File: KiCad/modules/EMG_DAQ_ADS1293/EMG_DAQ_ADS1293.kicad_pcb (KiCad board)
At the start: 2 copper layers, 15 x 9.5 mm, 27 parts, among them J1 Conn_01x01_Pin, J10 Conn_01x01_Pin, J11 Conn_01x01_Pin, J12 Conn_01x01_Pin, J13 Conn_01x01_Pin, J14 Conn_01x01_Pin, J15 Conn_01x01_Pin, J16 Conn_01x01_Pin, J2 Conn_01x01_Pin, J3 Conn_01x01_Pin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

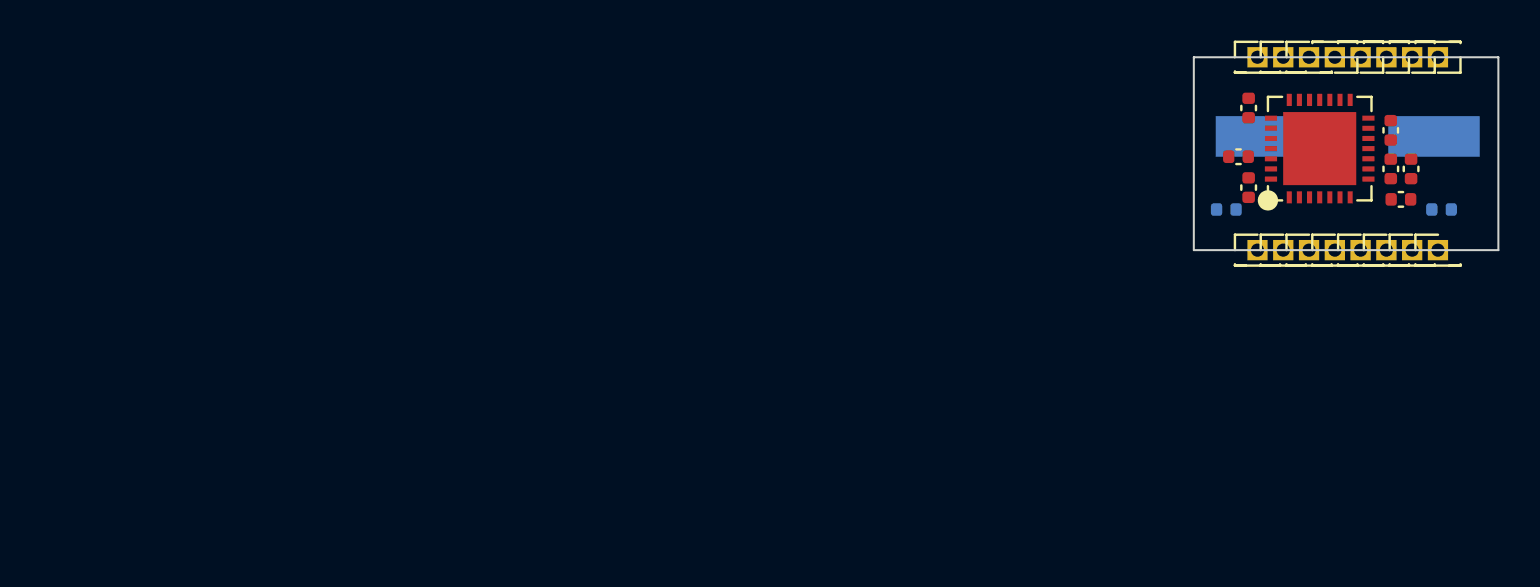
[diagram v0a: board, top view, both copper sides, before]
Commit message: reshaped the modules boards sizes
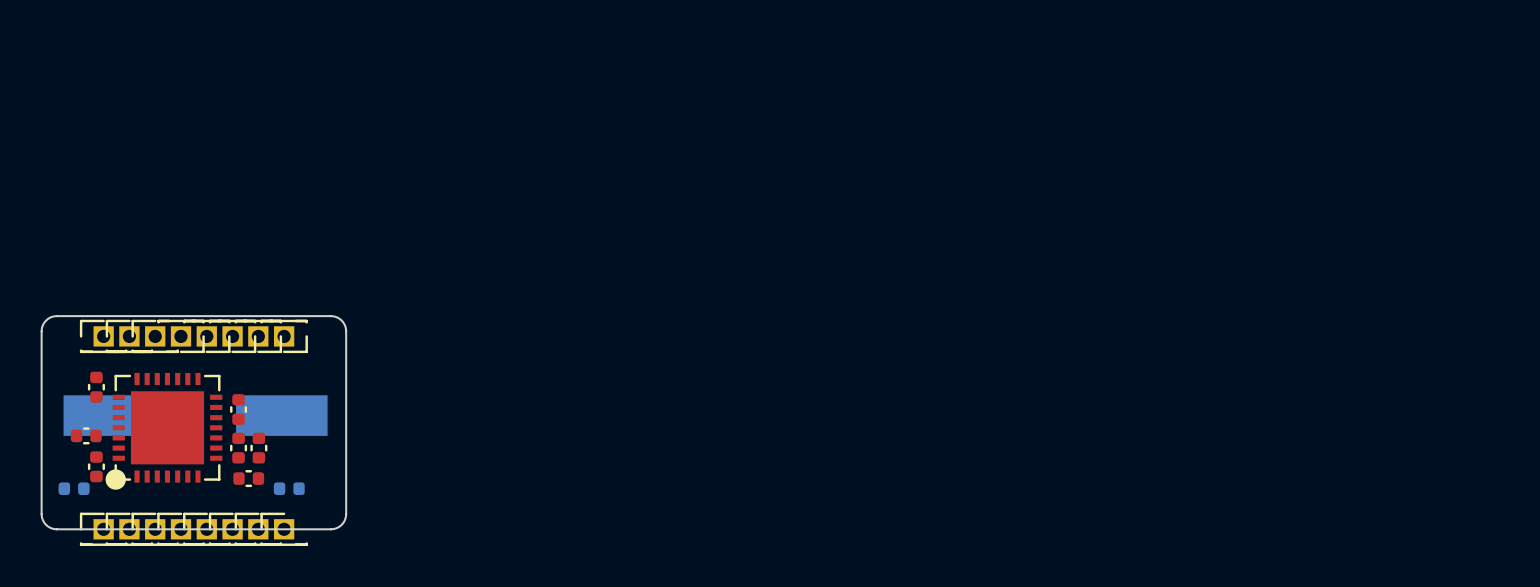
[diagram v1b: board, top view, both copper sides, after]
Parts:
- moved J11 58.5 mm to (104.4, 100.0)
- moved J12 58.5 mm to (98.1, 100.0)
- moved J16 58.5 mm to (104.4, 109.5)
- moved J3 58.5 mm to (98.1, 109.5)
- moved J6 58.5 mm to (101.9, 109.5)
- moved J9 58.5 mm to (101.9, 100.0)
- moved J10 58.5 mm to (103.2, 100.0)
- moved J14 58.5 mm to (96.8, 100.0)
- moved J15 58.5 mm to (103.2, 109.5)
- moved J2 58.5 mm to (96.8, 109.5)
- moved J4 58.5 mm to (99.4, 109.5)
- moved J5 58.5 mm to (100.6, 109.5)
- moved J7 58.5 mm to (99.4, 100.0)
- moved J8 58.5 mm to (100.6, 100.0)
- moved J1 58.5 mm to (95.6, 109.5)
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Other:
- board size 15 x 9.5 mm -> 15 x 10.5 mm
- copper layers 2 -> 4

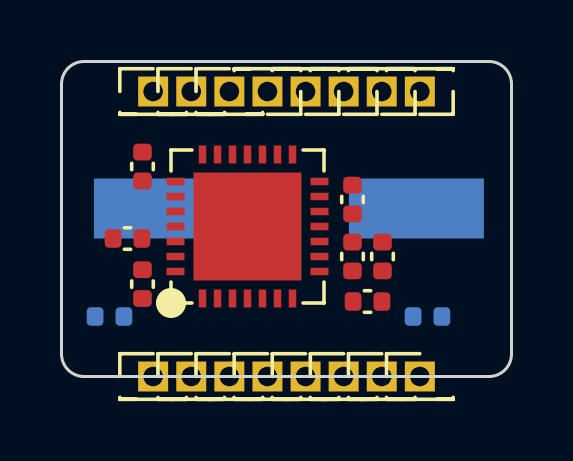
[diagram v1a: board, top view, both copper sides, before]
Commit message: some cleaning + edge plating dry electrode
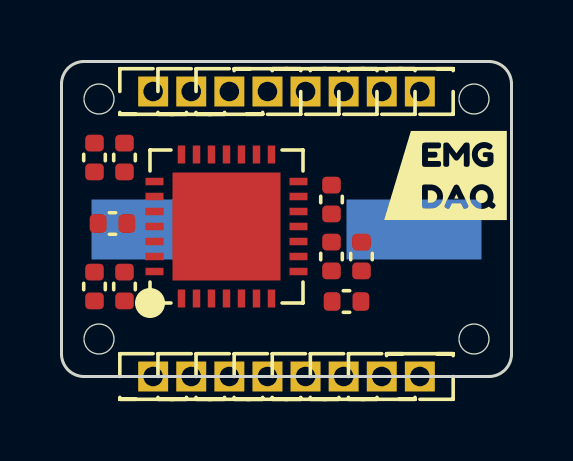
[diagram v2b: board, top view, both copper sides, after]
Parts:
- added kibuzzard-6569F40D: G***, kibuzzard-6569F40D, F.Cu at (105.3, 102.8)
- C1, C2: moved to F.Cu
- moved C2 11.1 mm to (93.6, 106.5), turned to -90 degrees
- moved C4 2.92 mm to (93.6, 102.2), turned to -90 degrees
- moved C3 2.25 mm to (94.2, 104.4), turned to 0 degrees
- moved C1 1.12 mm to (94.6, 106.5), turned to 90 degrees
- moved Y1 0.70 mm to (100.0, 104.6)
- moved C6 0.70 mm to (101.5, 105.5)
- moved C7 0.70 mm to (101.5, 103.6)
- moved R1 0.70 mm to (102.0, 107.0)
- moved R2 0.70 mm to (102.5, 105.5)
- moved U1 0.70 mm to (98.0, 104.5)
- moved C5 0.67 mm to (94.6, 102.2)
- turned J16 to 180 degrees
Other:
- outline, holes or cut-outs redrawn
- board text added: "By Aightech"

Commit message: finished rooting emgdaq + schematic commod
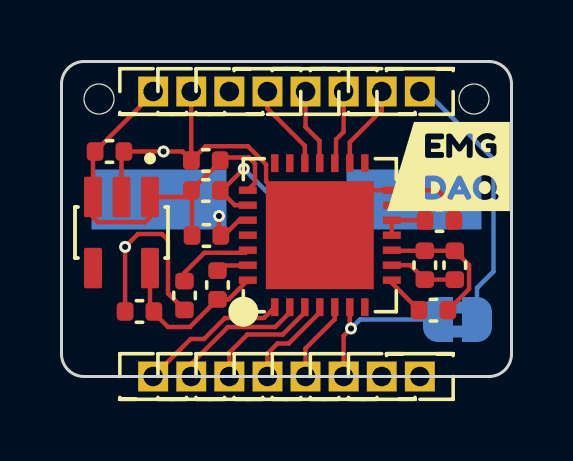
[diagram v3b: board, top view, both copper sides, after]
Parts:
- added C8: 1uF, Capacitor_SMD:C_0402_1005Metric, F.Cu at (95.1, 107.3)
- added C9: 1uF, Capacitor_SMD:C_0402_1005Metric, F.Cu at (94.1, 102.0)
- added JP2: SolderJumper_2_Bridged, Jumper:SolderJumper-2_P1.3mm_Bridged2Bar_RoundedPad1.0x1.5mm, B.Cu at (105.7, 107.6)
- added U2: AP2112K-3.3TRG1, 00_custom-footprints:SOT95P285X140-5N, F.Cu at (94.5, 104.7)
- moved J1 9.83 mm to (98.1, 100.0)
- moved J8 9.58 mm to (101.9, 109.5), turned to 0 degrees
- moved J12 5.08 mm to (103.2, 100.0)
- moved J7 5.08 mm to (104.4, 100.0)
- moved C4 3.87 mm to (97.3, 103.3), turned to 0 degrees
- moved C7 3.67 mm to (105.1, 104.3), turned to 0 degrees
- moved C3 3.16 mm to (97.3, 104.8)
- moved C6 3.12 mm to (104.6, 105.8)
- moved R2 3.12 mm to (105.6, 105.8)
- moved U1 3.12 mm to (101.1, 104.8)
- moved C1 3.10 mm to (97.7, 106.5)
- moved C2 3.01 mm to (96.6, 106.8)
- moved R1 2.91 mm to (104.9, 107.3)
- moved C5 2.71 mm to (97.3, 102.3), turned to 180 degrees
- moved J9 2.54 mm to (99.4, 100.0)
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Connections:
- net /+5VA renamed +3.3VA
- net Net-(J10-Pin_1) renamed /MOSI
- net Net-(J11-Pin_1) renamed /SCLK
- net Net-(J12-Pin_1) renamed /CSB
- net Net-(J9-Pin_1) renamed /MISO
- J1 pad 1: GND -> unconnected-(J1-Pin_1-Pad1)
- J13 pad 1: +5V -> +3.3V
- J7 pad 1: /in6 -> /extRef
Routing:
- net GND: track 0.00 -> 24.4 mm, vias 0 -> 2
- net +3.3V: track 0.00 -> 14.5 mm
- net /extRef: track 0.00 -> 8.96 mm
- net XTAL1: track 0.00 -> 8.31 mm, vias 0 -> 1
- net +3.3VA: track 0.00 -> 5.52 mm
- net /in6: track 0.00 -> 5.37 mm, vias 0 -> 1
- net /in1: track 0.00 -> 5.01 mm
- net /RLDINV: track 0.00 -> 4.58 mm
- net /in2: track 0.00 -> 4.51 mm
- net XTAL2: track 0.00 -> 4.16 mm, vias 0 -> 1
- net /in3: track 0.00 -> 3.96 mm
- net /in4: track 0.00 -> 3.17 mm
- net /MISO: track 0.00 -> 2.91 mm
- net /CSB: track 0.00 -> 2.83 mm
- net /cvref: track 0.00 -> 2.70 mm
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- added copper zone on In1.Cu, net GND
- added copper zone on In2.Cu, net GND
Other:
- outline, holes or cut-outs redrawn
- board text added: "Aightech"
- board text removed: "By Aightech"

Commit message: lot of updates on ads93,flex,commod,pad
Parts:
- removed kibuzzard-6569F40D: G***, kibuzzard-6569F40D
- added kibuzzard-658D7E24: G***, kibuzzard-658D7E24, F.Cu at (31.7, 31.6)
- U1: footprint 00_custom-footprints:ADS1293CISQE -> 00_Custom:ADS1293CISQE
- U2: footprint 00_custom-footprints:SOT95P285X140-5N -> 00_Custom:SOT95P285X140-5N
- moved J1 99.0 mm to (28.1, 30.0)
- moved J10 99.0 mm to (30.6, 30.0)
- moved J11 99.0 mm to (31.9, 30.0)
- moved J12 99.0 mm to (33.2, 30.0)
- moved J13 99.0 mm to (25.6, 30.0)
- moved J14 99.0 mm to (26.8, 30.0)
- moved J7 99.0 mm to (34.4, 30.0)
- moved J9 99.0 mm to (29.4, 30.0)
- moved C1 98.6 mm to (27.7, 37.0)
- moved C2 98.6 mm to (26.6, 37.3)
- moved C3 98.6 mm to (27.3, 35.3)
- moved C4 98.6 mm to (27.3, 33.8)
- moved C5 98.6 mm to (27.3, 32.8)
- moved C6 98.6 mm to (34.6, 36.3)
- moved C7 98.6 mm to (35.1, 34.8)
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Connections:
- J15 pad 1: unconnected-(J15-Pin_1-Pad1) -> /in4
- J16 pad 1: unconnected-(J16-Pin_1-Pad1) -> /in5
- J3 pad 1: /in2 -> /in1
- J4 pad 1: /in3 -> /in2
- J5 pad 1: /in4 -> /in2
- J6 pad 1: /in5 -> /in3
- J8 pad 1: /in6 -> /in3
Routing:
- net /in6: track 5.37 -> 3.34 mm
- net /in5: track 2.63 -> 4.19 mm
- net /in1: track 5.01 -> 6.20 mm
- net /CSB: track 2.83 -> 3.33 mm
- added copper zone on B.Cu, net GND
- added copper zone on F.Cu, net GND
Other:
- board size 15 x 10.5 mm -> 15 x 11 mm
- board text added: "by Aightech"
- board text removed: "Aightech"

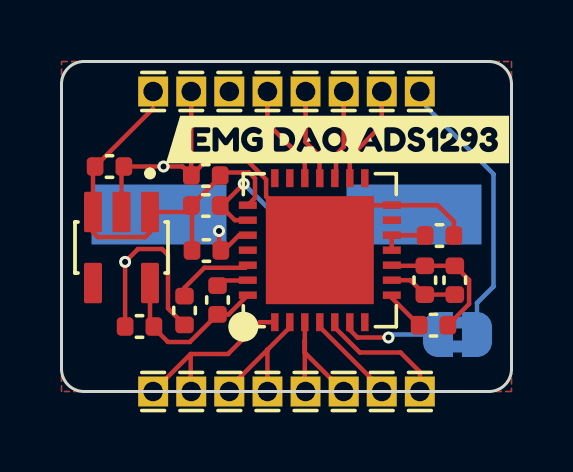
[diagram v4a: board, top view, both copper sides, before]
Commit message: finished ads93,commod,drypad,flexpad,jackconn,imubno + plot and render
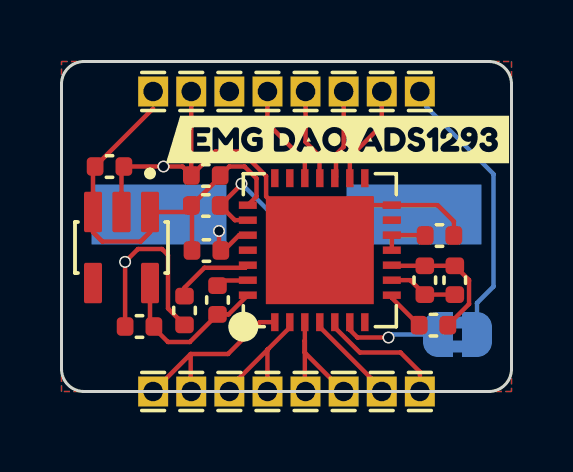
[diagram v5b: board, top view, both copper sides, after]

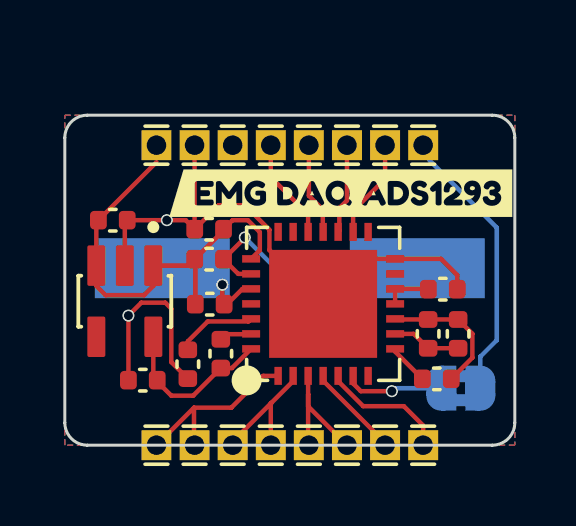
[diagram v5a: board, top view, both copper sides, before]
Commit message: refactor and fixing most of the modules
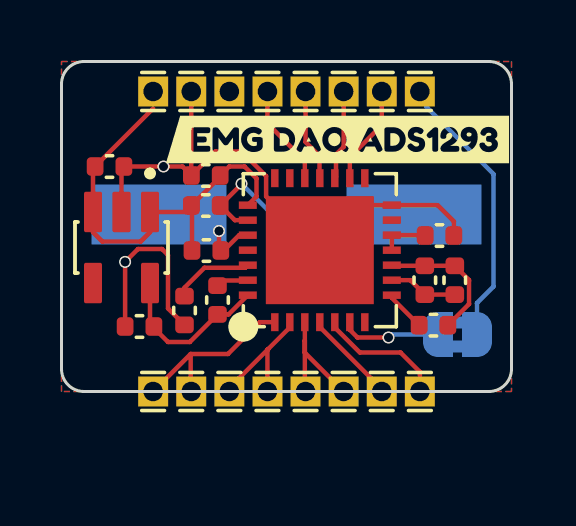
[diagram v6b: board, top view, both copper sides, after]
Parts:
- moved JP2 1.79 mm to (35.6, 36.3)
- moved C1 1.79 mm to (27.6, 35.2)
- moved U2 1.79 mm to (24.4, 33.4)
- moved Y1 1.79 mm to (29.9, 32.3)
- moved C9 1.79 mm to (24.0, 30.7)
- moved J10 1.79 mm to (30.5, 28.2)
- moved J11 1.79 mm to (31.8, 28.2)
- moved J7 1.79 mm to (34.3, 28.2)
- moved J1 1.79 mm to (28.0, 28.2)
- moved J12 1.79 mm to (33.1, 28.2)
- moved J13 1.79 mm to (25.4, 28.2)
- moved J14 1.79 mm to (26.7, 28.2)
- moved J9 1.79 mm to (29.3, 28.2)
- moved kibuzzard-658D7E24 1.79 mm to (31.6, 29.8)
- moved C2 1.79 mm to (26.5, 35.5)
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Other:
- outline, holes or cut-outs redrawn

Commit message: cleaned all modules + production files
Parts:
- U2: footprint 00_Custom:SOT95P285X140-5N -> 00_lcsc:SOT-25-5_L2.9-W1.6-P0.95-LS2.8-BL
- moved U2 0.11 mm to (24.5, 33.5), turned to 180 degrees
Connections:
- U2 pad 4: (no net) -> unconnected-(U2-NC-Pad4)

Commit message: renamed SPI buses
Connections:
- net /MISO renamed /POCI
- net /MOSI renamed /PICO
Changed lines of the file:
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@@
 	(net 24 "/extRef")
 	(net 25 "unconnected-(J1-Pin_1-Pad1)")
-	(net 26 "/MISO")
-	(net 27 "/MOSI")
+	(net 26 "/POCI")
+	(net 27 "/PICO")
 	(net 28 "/SCLK")
 	(net 29 "/CSB")
@@
 			(layers "*.Cu" "*.Mask")
 			(remove_unused_layers no)
-			(net 26 "/MISO")
+			(net 26 "/POCI")
 			(pinfunction "Pin_1")
 			(pintype "passive")
@@
 			(size 0.25 0.6)
 			(layers "F.Cu" "F.Paste" "F.Mask")
-			(net 27 "/MOSI")
+			(net 27 "/PICO")
 			(pinfunction "SDI")
 			(pintype "input")
@@
 			(size 0.25 0.6)
 			(layers "F.Cu" "F.Paste" "F.Mask")
-			(net 26 "/MISO")
+			(net 26 "/POCI")
 			(pinfunction "SDO")
 			(pintype "output")
@@
 			(layers "*.Cu" "*.Mask")
 			(remove_unused_layers no)
-			(net 27 "/MOSI")
+			(net 27 "/PICO")
 			(pinfunction "Pin_1")
 			(pintype "passive")
